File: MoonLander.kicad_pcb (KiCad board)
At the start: 4 copper layers, 41.5 x 23.2 mm, 56 parts, among them IC201 BQ24040/5, IC202 BU33SD5, IC301 PRTR5V0U2X, IC302 CP2110-GM, IC401 HDC1008, IC402 TSL4531, IC601 LPC824M201JHI33, J601 Cortex_JTAG/SWD_10, P101 CONN_01X02, P102 CONN_01X02, P103 USB_OTG, P501 CONN_02X08, SW501 SW_PUSH, SW502 SW_PUSH, Y601 Crystal

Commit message: moved some things around
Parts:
- moved R601 16.5 mm to (150.1, 101.6)
- moved R602 16.5 mm to (151.6, 101.6)
- moved IC601 16.4 mm to (157.4, 99.7)
- moved P501 16.4 mm to (167.4, 110.1)
- moved C401 16.4 mm to (158.8, 89.7)
- moved C402 16.4 mm to (164.7, 90.8)
- moved D201 16.4 mm to (133.1, 97.4)
- moved P103 16.4 mm to (129.5, 105.5)
- moved R204 16.4 mm to (143.3, 98.9)
- moved Y601 16.4 mm to (156.3, 105.2)
- moved C201 16.4 mm to (136.9, 97.7)
- moved C302 16.4 mm to (136.9, 107.6)
- moved D203 16.4 mm to (133.6, 90.8)
- moved FB101 16.4 mm to (133.7, 103.6)
- moved IC301 16.4 mm to (134.6, 108.1)
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
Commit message: routing complete
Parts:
- moved R17 12.8 mm to (153.4, 109.7)
- moved R13 4.45 mm to (147.6, 106.3), turned to 270 degrees
- moved R12 3.73 mm to (149.1, 106.3), turned to 270 degrees
- moved C3 2.50 mm to (149.4, 96.1)
- moved C11 1.91 mm to (157.7, 93.5), turned to 90 degrees
- moved R18 1.83 mm to (159.3, 93.6), turned to 270 degrees
- moved C10 1.40 mm to (161.4, 105.0)
- moved Y1 1.15 mm to (155.2, 105.0)
- moved R11 1.05 mm to (146.1, 106.3), turned to 270 degrees
- moved C13 1.02 mm to (158.1, 105.0)
- moved C12 0.90 mm to (151.9, 104.3)
- moved C14 0.76 mm to (159.8, 105.0)
- moved R8 0.68 mm to (147.4, 101.7), turned to 0 degrees
- moved R16 0.60 mm to (154.9, 109.7)
- moved J1 0.38 mm to (156.8, 109.6)
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- renumbered C201 to C1, C601 to C10, C605 to C11, C603 to C12, C604 to C13, C602 to C14, C606 to C15, C202 to C2, C204 to C3, C301 to C4, C302 to C5, C303 to C6, C304 to C7, C401 to C8, C402 to C9, D201 to D1, D202 to D2, D203 to D3, D501 to D4, FB101 to FB1, IC201 to IC1, IC202 to IC2, IC301 to IC3, IC302 to IC4, IC401 to IC5, IC402 to IC6, IC601 to IC7, J601 to J1, P101 to P1, P102 to P2, P103 to P3, P501 to P4, R201 to R1, R401 to R10, R501 to R11, R502 to R12, R503 to R13, R601 to R14, R602 to R15, R603 to R16, R604 to R17, R605 to R18, R606 to R19, R202 to R2, R607 to R20, R608 to R21, R203 to R3, R204 to R4, R205 to R5, R206 to R6, R207 to R7, R208 to R8, R301 to R9, SW501 to SW1, SW502 to SW2, Y601 to Y1
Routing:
- net GND: track 0.00 -> 51.3 mm, vias 0 -> 28
- net /CPU/I2C0_SCL: track 0.00 -> 51.2 mm, vias 0 -> 1
- net /CPU/I2C0_SDA: track 0.00 -> 46.7 mm, vias 0 -> 2
- net VCC: track 0.00 -> 38.6 mm, vias 0 -> 8
- net /CPU/RH_DRDY: track 0.00 -> 35.6 mm, vias 0 -> 2
- net /CPU/ISP_RXD: track 0.00 -> 29.4 mm, vias 0 -> 2
- net /CPU/PIO0_16: track 0.00 -> 26.2 mm, vias 0 -> 1
- net /CPU/RH_PWR: track 0.00 -> 26.2 mm, vias 0 -> 2
- net /CPU/LUX_PWR: track 0.00 -> 22.6 mm, vias 0 -> 2
- net /CPU/RESET: track 0.00 -> 22.4 mm, vias 0 -> 1
- net /CPU/PIO0_15: track 0.00 -> 22.4 mm, vias 0 -> 2
- net /CPU/ISP_TXD: track 0.00 -> 22.0 mm, vias 0 -> 2
- net /CPU/SWCLK: track 0.00 -> 19.4 mm, vias 0 -> 1
- net /CPU/ISP_ENTRY: track 0.00 -> 18.1 mm, vias 0 -> 2
- net /CPU/LED_R: track 0.00 -> 17.7 mm, vias 0 -> 2
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- added copper zone on F.Cu, net GND
- added copper zone on F.Cu, net VCC
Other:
- rule trace_min: 0.2 -> 0.1524

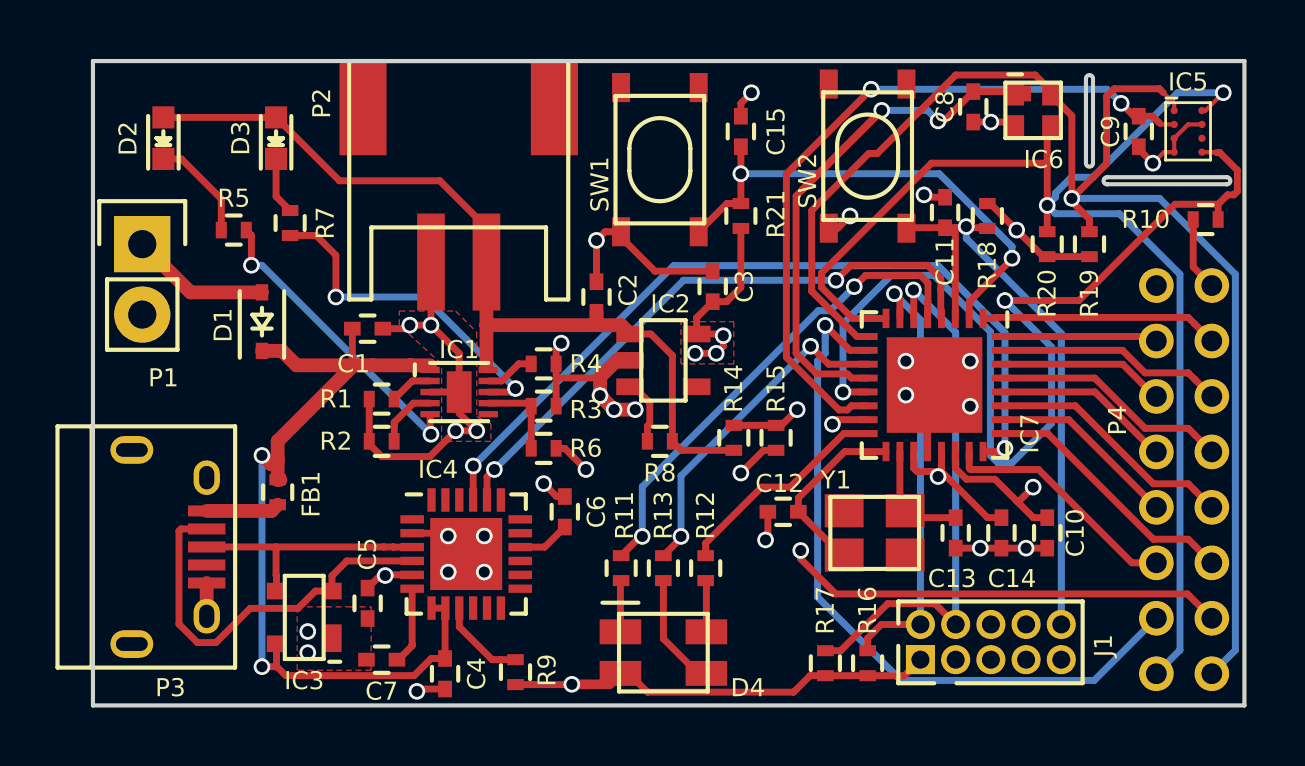
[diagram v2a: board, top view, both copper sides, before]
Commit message: moved header to connect fills below
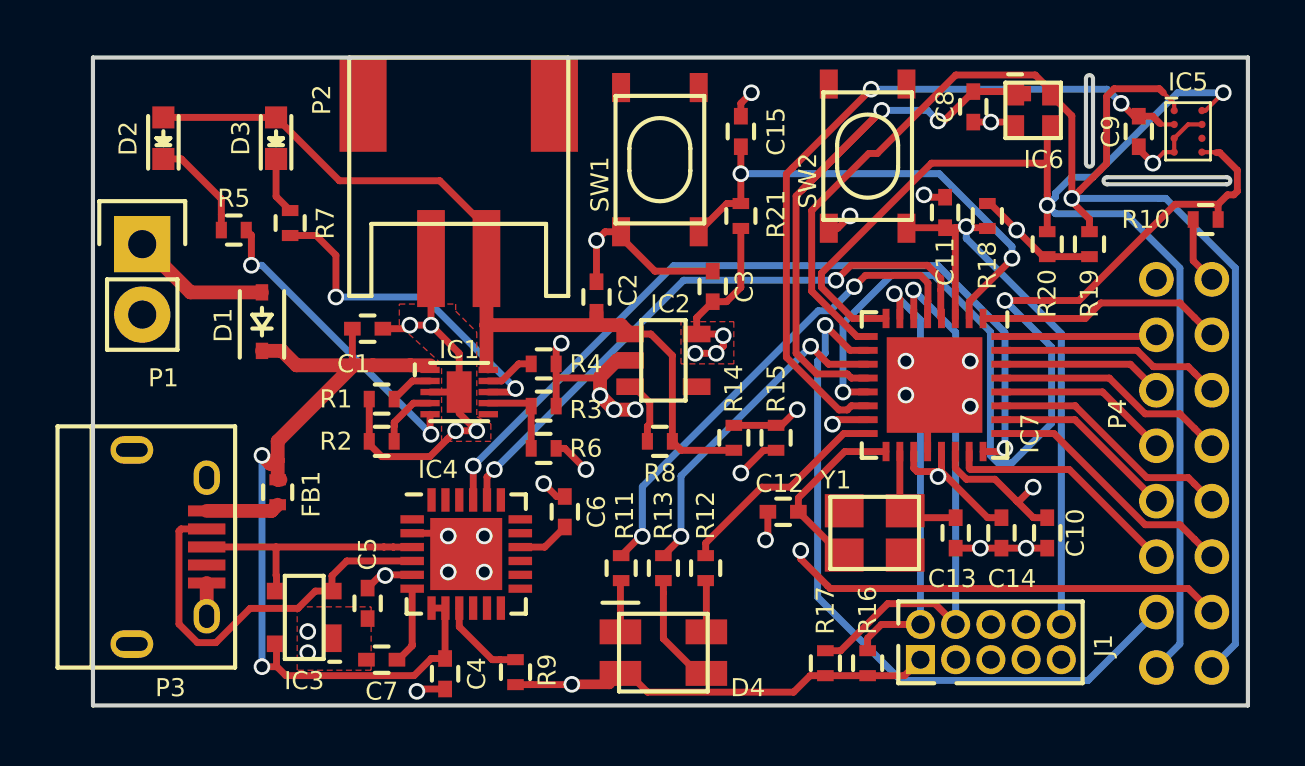
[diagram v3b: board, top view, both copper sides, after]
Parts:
- moved P4 0.22 mm to (167.4, 109.9)
- moved P2 0.13 mm to (140.2, 87.9)
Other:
- board size 41.5 x 23.2 mm -> 41.7 x 23.4 mm

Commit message: checking CircuitHub cost with 2 layers
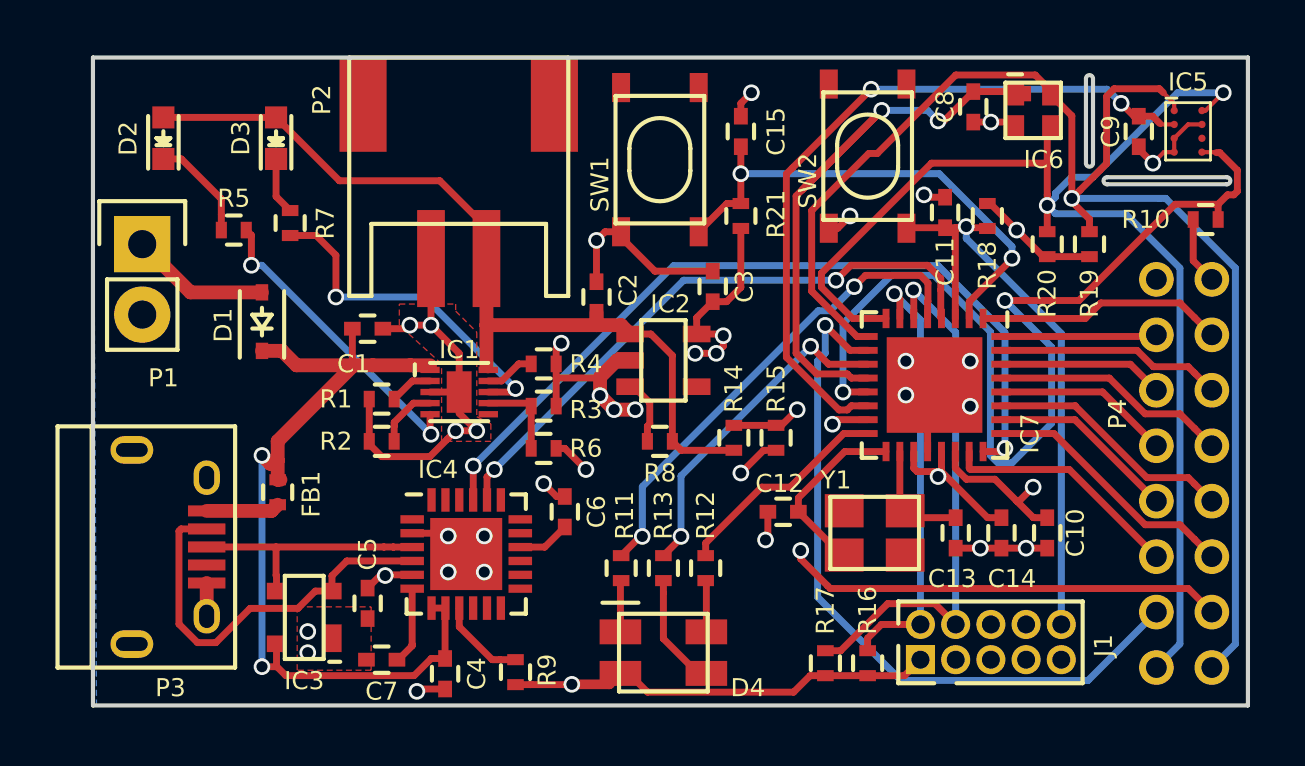
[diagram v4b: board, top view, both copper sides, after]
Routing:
- added copper zone on B.Cu, net GND
- removed copper zone on In1.Cu, net GND
- removed copper zone on F.Cu, net VCC
- removed copper zone on In2.Cu, net VCC
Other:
- copper layers 4 -> 2
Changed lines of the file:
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@@
-(kicad_pcb (version 4) (host pcbnew 0.201512021501+6340~38~ubuntu15.10.1-stable)
+(kicad_pcb (version 4) (host pcbnew 0.201512051502+6347~38~ubuntu15.10.1-stable)
   (general
     (links 154)
     (no_connects 2)
-    (area 123.715 74.186 171.362334 117.633144)
+    (area 123.715 74.059 171.362334 117.633144)
     (thickness 1.6)
     (drawings 12)
@@
   (layers
     (0 F.Cu signal)
-    (1 In1.Cu signal)
-    (2 In2.Cu signal)
     (31 B.Cu signal)
     (33 F.Adhes user)
@@
   (segment (start 141.69 109.601) (end 142.24 109.601) (width 0.25) (layer F.Cu) (net 55))
   (segment (start 140.208 107.745) (end 140.212 107.741) (width 0.25) (layer F.Cu) (net 55))
-  (zone (net 2) (net_name GND) (layer In1.Cu) (hatch edge 0.508)
+  (zone (net 2) (net_name GND) (layer B.Cu) (hatch edge 0.508)
     (connect_pads (clearance 0.125))
     (min_thickness 0.254)
@@
       )
     )
-  )
-  (zone (net 4) (net_name VCC) (layer In2.Cu) (hatch edge 0.508)
-    (connect_pads (clearance 0.125))
-    (min_thickness 0.254)
-    (fill yes (arc_segments 16) (thermal_gap 0.508) (thermal_bridge_width 0.508))
-    (polygon
-      (pts
-        (xy 127 87.884) (xy 168.656 87.884) (xy 168.656 111.252) (xy 127 111.252)
-      )
-    )
-  )
-  (zone (net 4) (net_name VCC) (layer F.Cu) (hatch edge 0.508)
-    (connect_pads yes (clearance 0.125))
-    (min_thickness 0.254)
-    (fill yes (arc_segments 16) (thermal_gap 0.508) (thermal_bridge_width 0.508))
-    (polygon
-      (pts
-        (xy 148.209 97.409) (xy 150.114 97.409) (xy 150.114 98.933) (xy 148.209 98.933)
-      )
-    )

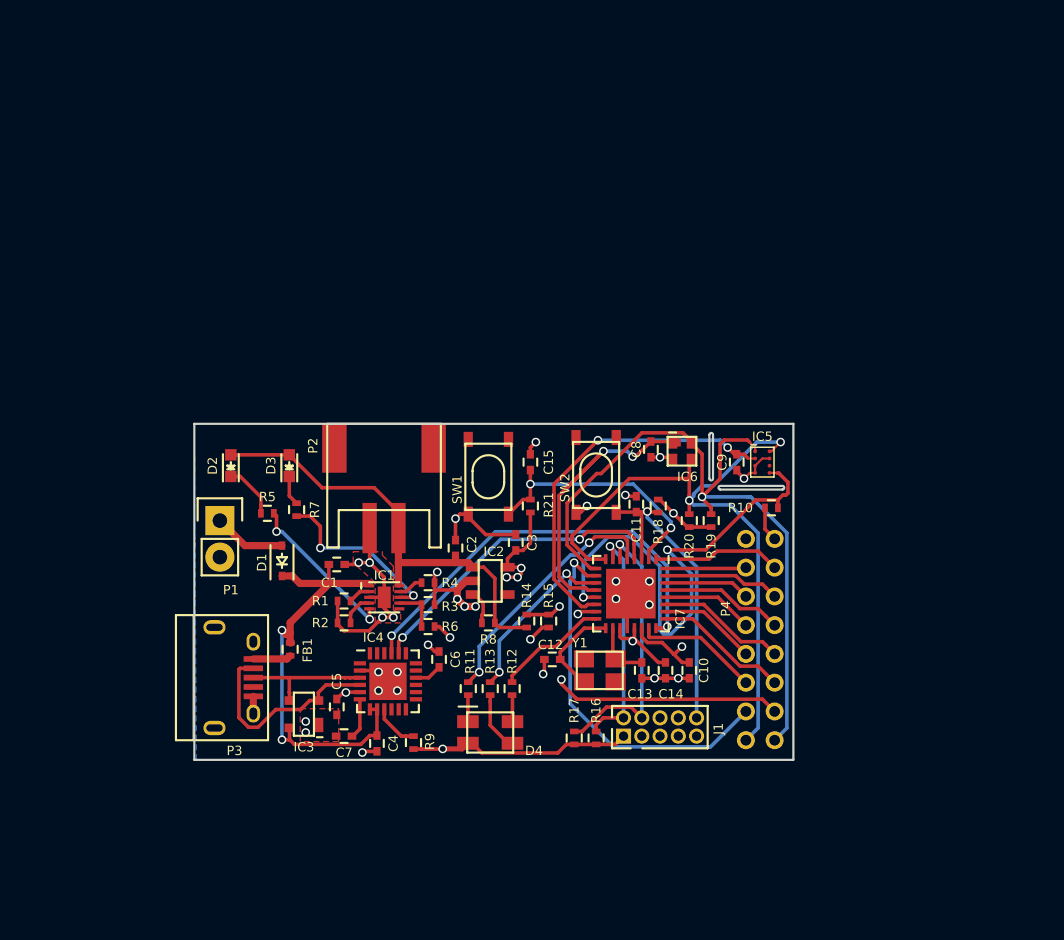
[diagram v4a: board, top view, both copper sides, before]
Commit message: simplified 2 layer version
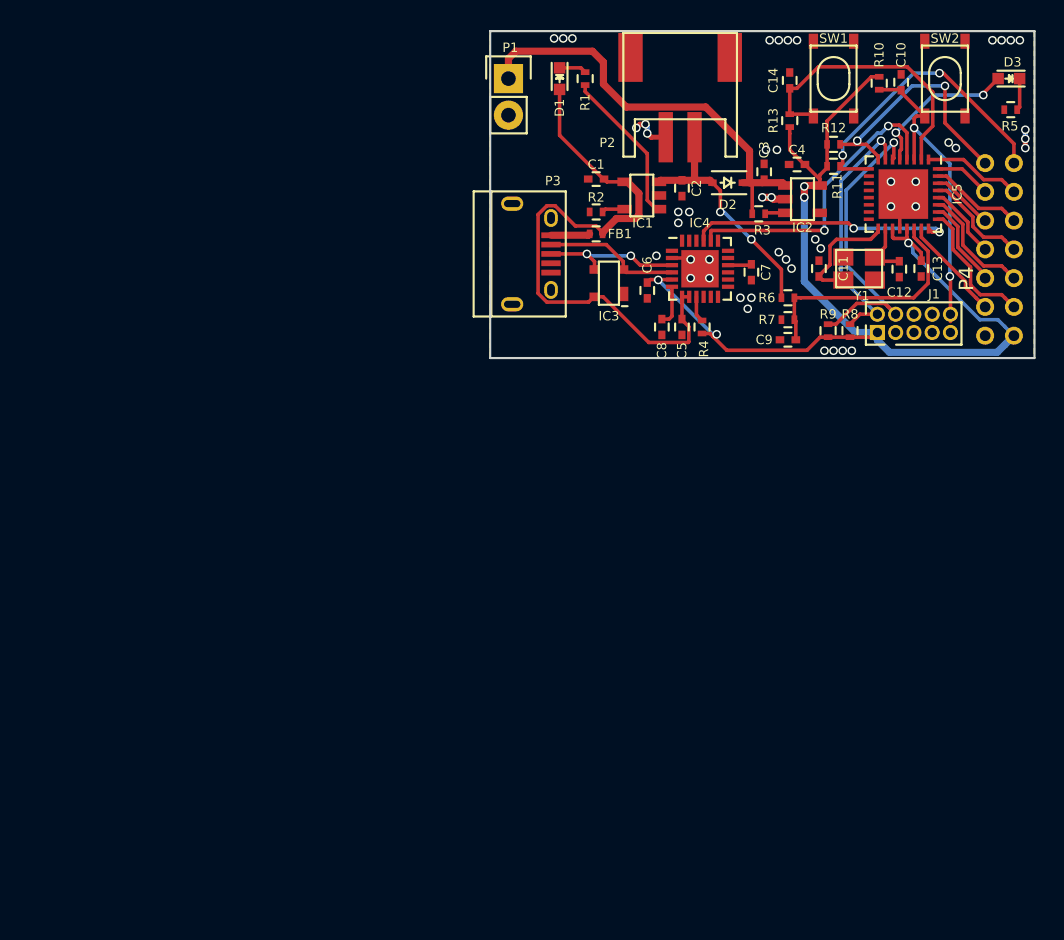
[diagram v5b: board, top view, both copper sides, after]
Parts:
- removed C15: 0.1uF, Capacitors_SMD:C_0402
- removed D4: LED_RABG, GrayCatLabs:PLCC4
- removed IC6: TSL4531, GrayCatLabs:TSL4531
- removed IC7: LPC824M201JHI33, Housings_DFN_QFN:QFN-32-1EP_5x5mm_Pitch0.5mm
- removed R14, R15, R21: 100k, Resistors_SMD:R_0402
- removed R16, R17, R18, R19, R20: 10k, Resistors_SMD:R_0402
- C11: value 0.1uF -> 18pF
- C13: value 18pF -> 0.1uF
- C5, C8: value 0.1uF -> 1uF
- C6: value 4.7uF -> 0.1uF
- C7: value 1uF -> 4.7uF
- D1: value D_Schottky -> LED; footprint Diodes_SMD:SOD-323 -> LEDs:LED-0603
- D2: value LED -> D_Schottky; footprint LEDs:LED-0603 -> Diodes_SMD:SOD-323
- IC1: value BQ24040/5 -> MCP73831/2; footprint GrayCatLabs:TI-DSQ -> GrayCatLabs:SSOP5
- IC5: value HDC1008 -> LPC824M201JHI33; footprint GrayCatLabs:TI-YPA0008 -> Housings_DFN_QFN:QFN-32-1EP_5x5mm_Pitch0.5mm
- P4: footprint GrayCatLabs:Header_2mm_2x8 -> GrayCatLabs:Header_2mm_2x6
- R10, R8: value 100k -> 10k
- R11, R12: value R -> 10k
- R13: value R -> 100k
- R2: value 2k -> 10k
- R5: value 1k -> 470
- R6: value 0 -> 100k
- R7: value 1k -> 100k
- moved R5 58.8 mm to (183.8, 66.0), turned to 180 degrees
- moved D3 56.8 mm to (183.6, 63.9), turned to 180 degrees
- moved C4 49.7 mm to (168.9, 69.8), turned to 180 degrees
- moved R13 44.7 mm to (168.4, 66.8), turned to 90 degrees
- moved R11 44.3 mm to (171.4, 70.0), turned to 0 degrees
- moved R12 44.0 mm to (171.4, 68.5), turned to 0 degrees
- moved C10 43.5 mm to (176.1, 64.1), turned to 90 degrees
- moved C7 42.9 mm to (165.7, 77.3), turned to 270 degrees
- moved C14 41.9 mm to (168.4, 64.0), turned to 90 degrees
- moved R9 40.6 mm to (171.1, 81.4)
- moved R1 40.0 mm to (154.2, 63.9), turned to 90 degrees
- moved D2 39.8 mm to (164.1, 71.1), turned to 180 degrees
- moved D1 38.7 mm to (152.4, 63.9), turned to 270 degrees
- moved IC3 36.7 mm to (155.8, 78.1)
- moved SW2 36.7 mm to (179.2, 63.9), turned to 0 degrees
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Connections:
- C10 pad 1: Net-(C10-Pad1) -> /CPU/RESET
- C11 pad 1: /CPU/RESET -> GND
- C11 pad 2: GND -> Net-(C11-Pad2)
- C13 pad 1: GND -> VCC
- C13 pad 2: Net-(C13-Pad2) -> GND
- C14 pad 1: VCC -> /CPU/ISP_ENTRY
- C3 pad 1: VCC -> /PowerSupply/V_EXT
- C4 pad 1: 5V_USB -> VCC
- C5 pad 1: VCC -> 5V_USB
- C6 pad 1: Net-(C6-Pad1) -> VCC
- C7 pad 1: GND -> Net-(C7-Pad1)
- C7 pad 2: Net-(C7-Pad2) -> GND
- C8 pad 1: /CPU/LUX_PWR -> GND
- C8 pad 2: GND -> Net-(C8-Pad2)
- C9 pad 1: /CPU/RH_PWR -> Net-(C9-Pad1)
- D1 pad 1: 5V_USB -> Net-(D1-Pad1)
- D1 pad 2: /PowerSupply/V_EXT -> 5V_USB
- D2 pad 1: Net-(D2-Pad1) -> /PowerSupply/V_EXT
- D3 pad 2: /CPU/V_BAT -> /CPU/LED
- IC1 pad 1: 5V_USB -> Net-(IC1-Pad1)
- IC1 pad 2: Net-(IC1-Pad2) -> GND
- IC1 pad 3: GND -> /CPU/V_BAT
- IC1 pad 4: Net-(IC1-Pad4) -> 5V_USB
- IC2 pad 1: /CPU/V_BAT -> /PowerSupply/V_EXT
- IC4 pad 16: Net-(C6-Pad1) -> Net-(C7-Pad1)
- IC4 pad 6: Net-(C7-Pad2) -> Net-(C8-Pad2)
- P4 pad 1: /CPU/I2C0_SCL -> VCC
- P4 pad 10: /CPU/PIO0_21/ADC_5 -> /CPU/PIO0_19/ADC_7
- P4 pad 11: /CPU/PIO0_18/ADC_8 -> /CPU/PIO0_13/ADC_10
- P4 pad 12: /CPU/PIO0_19/ADC_7 -> /CPU/PIO0_17/ADC_9
- P4 pad 13: /CPU/PIO0_13/ADC_10 -> /CPU/I2C0_SCL
- P4 pad 14: /CPU/PIO0_17/ADC_9 -> /CPU/I2C0_SDA
- P4 pad 2: /CPU/I2C0_SDA -> GND
- P4 pad 3: /CPU/PIO0_15 -> /CPU/PIO0_14/ADC_2
- P4 pad 4: /CPU/PIO0_16 -> /CPU/PIO0_6/ADC_1
- P4 pad 5: /CPU/PIO0_14/ADC_2 -> /CPU/PIO0_22/ADC_4
- P4 pad 6: /CPU/PIO0_6/ADC_1 -> /CPU/PIO0_23/ADC_3
- P4 pad 7: /CPU/PIO0_22/ADC_4 -> /CPU/PIO0_20/ADC_6
- P4 pad 8: /CPU/PIO0_23/ADC_3 -> /CPU/PIO0_21/ADC_5
- P4 pad 9: /CPU/PIO0_20/ADC_6 -> /CPU/PIO0_18/ADC_8
- R1 pad 1: Net-(IC1-Pad2) -> Net-(IC1-Pad1)
- R1 pad 2: GND -> Net-(D1-Pad1)
- R10 pad 1: /CPU/RH_DRDY -> VCC
- R10 pad 2: VCC -> /CPU/RESET
- R11 pad 1: /CPU/LED_R -> VCC
- R11 pad 2: Net-(D4-Pad1) -> /CPU/I2C0_SCL
- R12 pad 1: /CPU/LED_G -> VCC
- R12 pad 2: Net-(D4-Pad4) -> /CPU/I2C0_SDA
- R13 pad 1: /CPU/LED_B -> VCC
- R13 pad 2: Net-(D4-Pad3) -> /CPU/ISP_ENTRY
- R2 pad 1: Net-(IC1-Pad4) -> GND
- R2 pad 2: GND -> Net-(IC1-Pad5)
- R3 pad 1: Net-(IC1-Pad7) -> Net-(IC2-Pad3)
- R3 pad 2: GND -> /PowerSupply/V_EXT
- R4 pad 1: GND -> VCC
- R4 pad 2: Net-(IC1-Pad9) -> Net-(IC4-Pad9)
- R5 pad 1: Net-(D2-Pad1) -> Net-(D3-Pad1)
- R5 pad 2: Net-(IC1-Pad5) -> GND
- R6 pad 1: VCC -> /CPU/V_BAT
- R6 pad 2: Net-(IC1-Pad7) -> Net-(C9-Pad1)
- R7 pad 1: Net-(D3-Pad1) -> Net-(C9-Pad1)
- R7 pad 2: Net-(IC1-Pad8) -> GND
- R8 pad 1: Net-(IC2-Pad3) -> VCC
- R8 pad 2: /CPU/V_BAT -> /CPU/SWDIO
- R9 pad 2: Net-(IC4-Pad9) -> /CPU/SWCLK
- Y1 pad 1: Net-(C12-Pad2) -> Net-(C11-Pad2)
- Y1 pad 2: Net-(C13-Pad2) -> Net-(C12-Pad2)
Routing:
- net GND: track 51.3 -> 8.94 mm, vias 28 -> 47
- net VCC: track 38.4 -> 75.0 mm, vias 8 -> 5
- net /CPU/RH_DRDY: track 35.6 -> 0.00 mm, vias 2 -> 0
- net /CPU/I2C0_SCL: track 51.1 -> 21.0 mm, vias 1 -> 2
- net /CPU/I2C0_SDA: track 46.6 -> 17.7 mm
- net /CPU/PIO0_16: track 26.3 -> 0.00 mm, vias 1 -> 0
- net /CPU/RH_PWR: track 26.2 -> 0.00 mm, vias 2 -> 0
- net /PowerSupply/V_EXT: track 5.04 -> 29.9 mm
- net /CPU/LUX_PWR: track 22.6 -> 0.00 mm, vias 2 -> 0
- net /CPU/PIO0_15: track 22.3 -> 0.00 mm, vias 2 -> 0
- net /CPU/LED_R: track 17.7 -> 0.00 mm, vias 2 -> 0
- net Net-(C10-Pad1): track 17.6 -> 0.00 mm, vias 2 -> 0
- net Net-(C9-Pad1): track 0.00 -> 16.9 mm
- net (no net): track 0.00 -> 14.7 mm, vias 2 -> 0
- net /CPU/V_BAT: track 31.5 -> 17.0 mm, vias 0 -> 2
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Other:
- board size 41.7 x 23.4 mm -> 37.8 x 22.7 mm
